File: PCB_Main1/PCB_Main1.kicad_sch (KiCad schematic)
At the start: 32 parts, among them M78AR05-? M78AR05

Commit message: Do annotation
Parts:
- XH3: renamed from J?; value Conn_01x04_Female -> SD-UART
- gave numbers to parts that had none: 24
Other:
- moved on the sheet: XH5, XH6

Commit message: update PCB_Main1 & PCB_Main2
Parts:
- removed M78AR05-3: M78AR05, Converter_DCDC:Converter_DCDC_RECOM_R-78E-0.5_THT, symbol Regulator_Switching:R-78E5.0-0.5
- added UM78AR033-1: R-78E3.3-0.5, Converter_DCDC:Converter_DCDC_RECOM_R-78E-0.5_THT, symbol Regulator_Switching:R-78E3.3-0.5
- XH6: value ICS-UART -> TWELITE_GPS_UART
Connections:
- net GND: now also UM78AR033-1.2 (GND)
- net at D9.2 (A): now also UM78AR033-1.1 (IN)
- net at D13.1 (K): now also UM78AR033-1.3 (OUT)
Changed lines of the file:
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@@
+    )
+  )
+  (symbol (lib_id "Regulator_Switching:R-78E3.3-0.5") (at 68.58 131.445 0) (unit 1)
+    (in_bom yes) (on_board yes) (dnp no) (fields_autoplaced)
+    (property "Reference" "UM78AR033-1" (at 68.58 124.46 0)
+      (effects (font (size 1.27 1.27)))
+    )
+    (property "Value" "R-78E3.3-0.5" (at 68.58 127 0)
+      (effects (font (size 1.27 1.27)))
+    )
+    (property "Footprint" "Converter_DCDC:Converter_DCDC_RECOM_R-78E-0.5_THT" (at 69.85 137.795 0)
+      (effects (font (size 1.27 1.27) italic) (justify left) hide)
+    )
+    (property "Datasheet" "https://www.recom-power.com/pdf/Innoline/R-78Exx-0.5.pdf" (at 68.58 131.445 0)
+      (effects (font (size 1.27 1.27)) hide)
+    )
+    (pin "1")
+    (pin "2")
+    (pin "3")
+    (instances
+      (project "PCB_Main1"
+        (path "/19e4d529-dbb3-4f23-85c8-a29dd0c78a6a"
+          (reference "UM78AR033-1") (unit 1)
+        )
+      )
     )
   )
@@
     )
   )
-  (symbol (lib_id "Regulator_Switching:R-78E5.0-0.5") (at 68.58 131.445 0) (mirror y) (unit 1)
-    (in_bom yes) (on_board yes) (dnp no) (fields_autoplaced)
-    (property "Reference" "M78AR05-3" (at 68.58 125.095 0)
-      (effects (font (size 1.27 1.27)))
-    )
-    (property "Value" "M78AR05" (at 68.58 127.635 0)
-      (effects (font (size 1.27 1.27)))
-    )
-    (property "Footprint" "Converter_DCDC:Converter_DCDC_RECOM_R-78E-0.5_THT" (at 67.31 137.795 0)
-      (effects (font (size 1.27 1.27) italic) (justify left) hide)
-    )
-    (property "Datasheet" "https://www.recom-power.com/pdf/Innoline/R-78Exx-0.5.pdf" (at 68.58 131.445 0)
-      (effects (font (size 1.27 1.27)) hide)
-    )
-    (pin "1")
-    (pin "2")
-    (pin "3")
-    (instances
-      (project "PCB_Main1"
-        (path "/19e4d529-dbb3-4f23-85c8-a29dd0c78a6a"
-          (reference "M78AR05-3") (unit 1)
-        )
-      )
-    )
-  )
   (symbol (lib_id "Regulator_Switching:R-78E5.0-0.5") (at 69.215 36.83 0) (mirror y) (unit 1)
     (in_bom yes) (on_board yes) (dnp no) (fields_autoplaced)
@@
   (symbol (lib_id "Regulator_Switching:R-78E5.0-0.5") (at 68.58 99.695 0) (mirror y) (unit 1)
     (in_bom yes) (on_board yes) (dnp no) (fields_autoplaced)
-    (property "Reference" "M78AR05-2" (at 68.58 93.345 0)
-      (effects (font (size 1.27 1.27)))
-    )
-    (property "Value" "M78AR05" (at 68.58 95.885 0)
+    (property "Reference" "M78AR05-2" (at 68.58 92.71 0)
+      (effects (font (size 1.27 1.27)))
+    )
+    (property "Value" "M78AR05" (at 68.58 95.25 0)
       (effects (font (size 1.27 1.27)))
     )
@@
   )
   (symbol (lib_id "Connector:Conn_01x05_Female") (at 80.01 167.005 0) (mirror y) (unit 1)
-    (in_bom yes) (on_board yes) (dnp no) (fields_autoplaced)
-    (property "Reference" "XH6" (at 78.105 165.735 0)
-      (effects (font (size 1.27 1.27)) (justify left))
-    )
-    (property "Value" "ICS-UART" (at 78.105 168.275 0)
-      (effects (font (size 1.27 1.27)) (justify left))
+    (in_bom yes) (on_board yes) (dnp no)
+    (property "Reference" "XH6" (at 69.215 165.1 0)
+      (effects (font (size 1.27 1.27)))
+    )
+    (property "Value" "TWELITE_GPS_UART" (at 69.215 167.64 0)
+      (effects (font (size 1.27 1.27)))
     )
     (property "Footprint" "" (at 80.01 167.005 0)

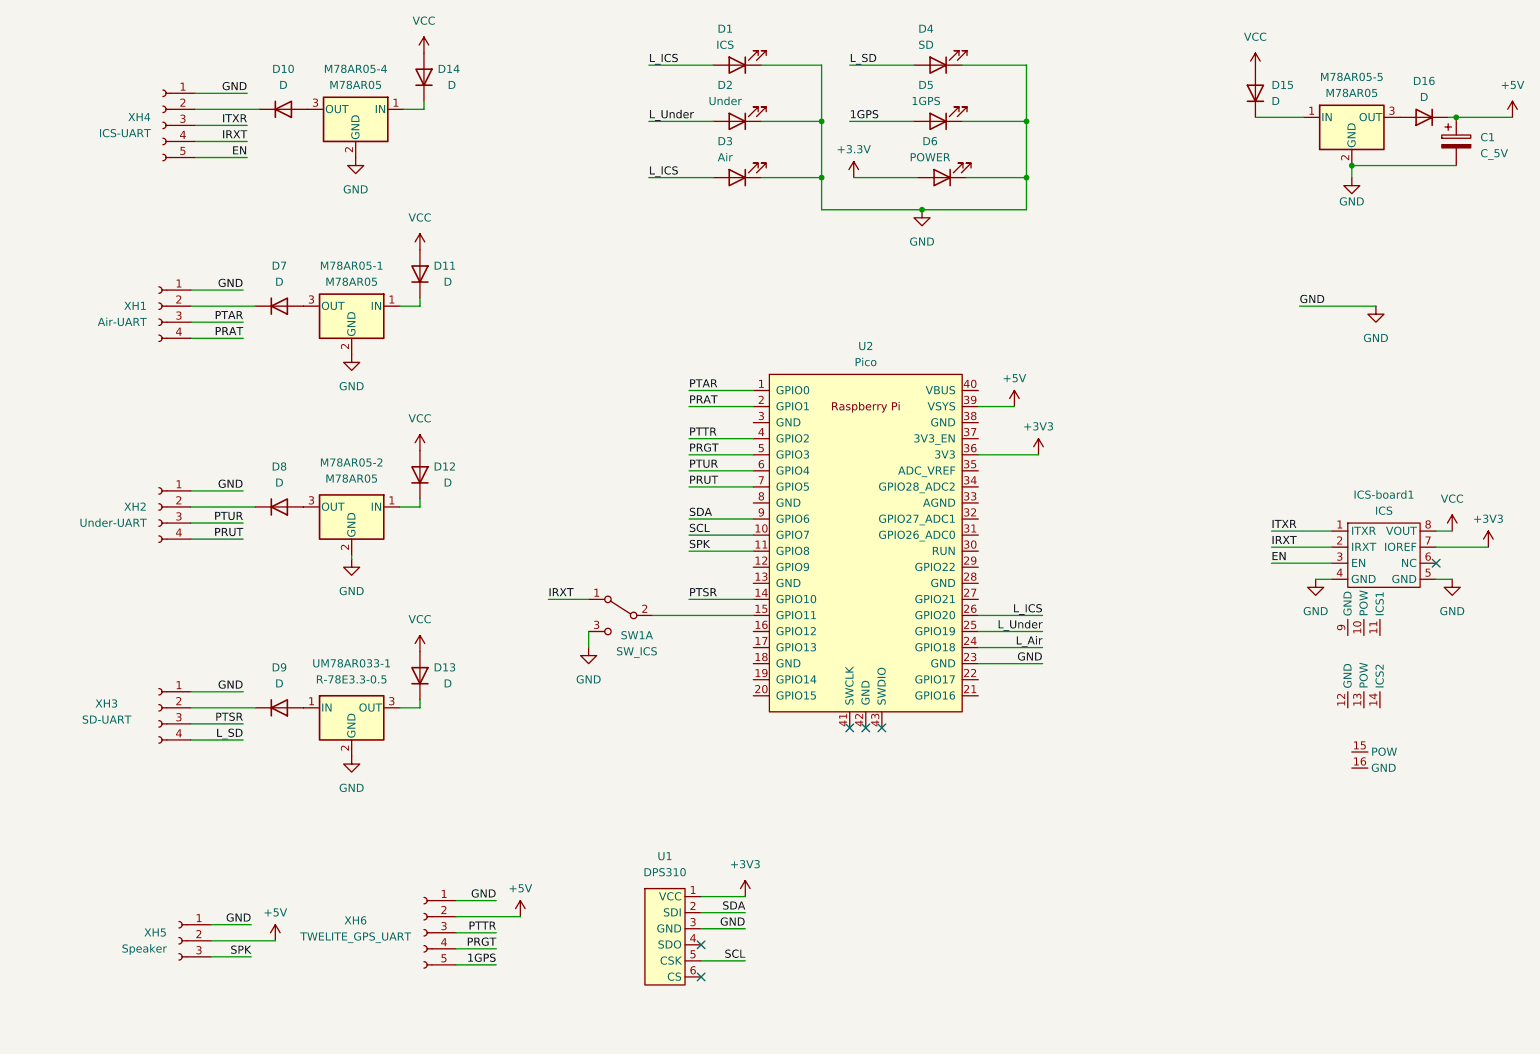
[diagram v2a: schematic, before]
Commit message: add gyro sensor
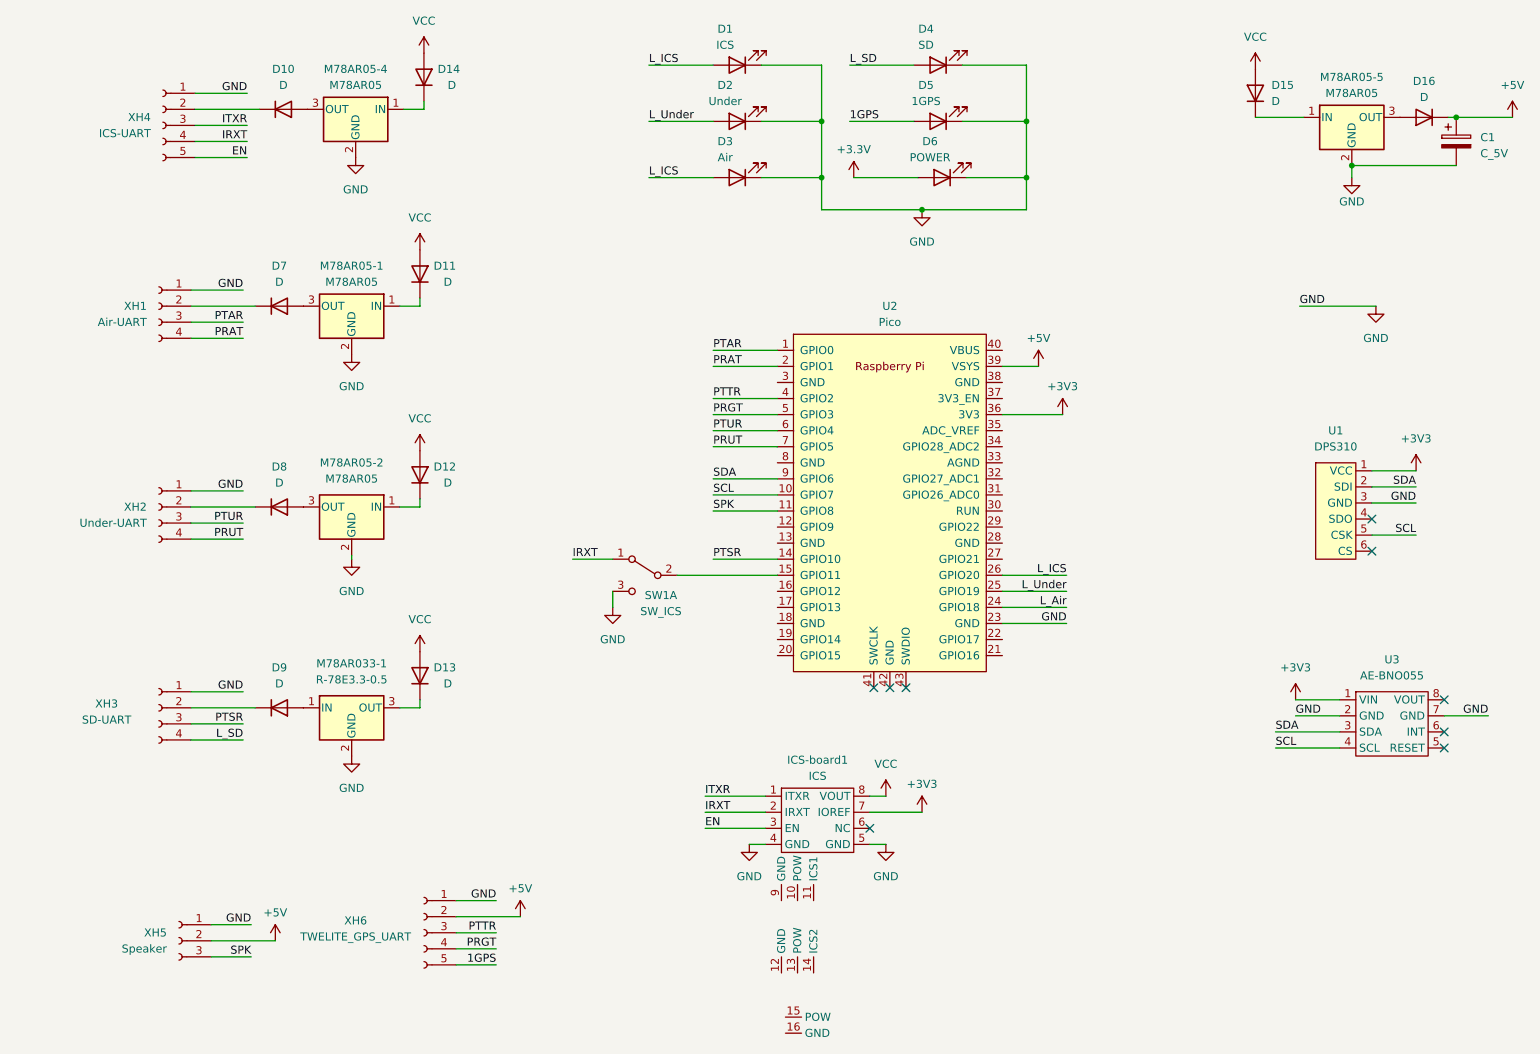
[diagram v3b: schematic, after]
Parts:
- added U3: AE-BNO055, symbol AE-BNO055:AE-BNO055
- renumbered UM78AR033-1 to M78AR033-1
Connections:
- net +3V3: now also U3.1 (VIN)
- net GND: now also U3.2 (GND), U3.7 (GND)
- net SCL: now also U3.4 (SCL)
- net SDA: now also U3.3 (SDA)
- no-connect marks 6 -> 9
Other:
- moved on the sheet: ICS-board1, SW1A, U1, U2

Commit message: update README.md
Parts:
- renumbered D7 to D1, D2 to D10, D3 to D11, D4 to D12, D5 to D13, D6 to D14, D8 to D2, D9 to D3, D10 to D4, D11 to D5, D12 to D6, D13 to D7, D14 to D8, D1 to D9, M78AR05-4 to M78AR05-3, M78AR05-5 to M78AR05-4, U2 to U1, U3 to U2, U1 to U3

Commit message: Update PCB_Main
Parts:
- C1: footprint (none) -> Capacitor_THT:CP_Radial_D5.0mm_P2.50mm
- D1, D15, D16, D2, D3, D4, D5, D6, D7, D8: footprint (none) -> Diode_THT:D_A-405_P10.16mm_Horizontal
- D10, D11, D12, D13, D14, D9: footprint (none) -> LED_THT:LED_D5.0mm
- ICS-board1: footprint (none) -> ICS:ICS
- SW1: footprint (none) -> Connector_PinHeader_2.54mm:PinHeader_1x03_P2.54mm_Vertical
- U1: footprint RPi_Pico:RPi_Pico_SMD_TH -> SamacSys_Parts:RPi_Pico_SMD_TH
- U2: footprint (none) -> AE-BNO055:AE-BNO055
- U3: footprint (none) -> DPS310:DPS310
- XH1, XH2, XH3: footprint (none) -> Connector_JST:JST_XH_S4B-XH-A_1x04_P2.50mm_Horizontal
- XH4, XH6: footprint (none) -> Connector_JST:JST_XH_S5B-XH-A_1x05_P2.50mm_Horizontal
- XH5: footprint (none) -> Connector_JST:JST_XH_S3B-XH-A_1x03_P2.50mm_Horizontal
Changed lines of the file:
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@@
       (effects (font (size 1.27 1.27)))
     )
-    (property "Footprint" "" (at 129.54 29.845 0)
+    (property "Footprint" "LED_THT:LED_D5.0mm" (at 129.54 29.845 0)
       (effects (font (size 1.27 1.27)) hide)
     )
@@
       (effects (font (size 1.27 1.27)))
     )
-    (property "Footprint" "" (at 57.15 131.445 0)
+    (property "Footprint" "Diode_THT:D_A-405_P10.16mm_Horizontal" (at 57.15 131.445 0)
       (effects (font (size 1.27 1.27)) hide)
     )
@@
       (effects (font (size 1.27 1.27)))
     )
-    (property "Footprint" "" (at 133.985 141.605 0)
+    (property "Footprint" "ICS:ICS" (at 133.985 141.605 0)
       (effects (font (size 1.27 1.27)) hide)
     )
@@
       (effects (font (size 1.27 1.27)) (justify right))
     )
-    (property "Footprint" "" (at 79.375 126.365 0)
+    (property "Footprint" "Diode_THT:D_A-405_P10.16mm_Horizontal" (at 79.375 126.365 0)
       (effects (font (size 1.27 1.27)) hide)
     )
@@
       (effects (font (size 1.27 1.27)))
     )
-    (property "Footprint" "" (at 38.1 131.445 0)
+    (property "Footprint" "Connector_JST:JST_XH_S4B-XH-A_1x04_P2.50mm_Horizontal" (at 38.1 131.445 0)
       (effects (font (size 1.27 1.27)) hide)
     )
@@
       (effects (font (size 1.27 1.27)) (justify left))
     )
-    (property "Footprint" "" (at 41.275 168.275 0)
+    (property "Footprint" "Connector_JST:JST_XH_S3B-XH-A_1x03_P2.50mm_Horizontal" (at 41.275 168.275 0)
       (effects (font (size 1.27 1.27)) hide)
     )
@@
       (effects (font (size 1.27 1.27)))
     )
-    (property "Footprint" "" (at 57.15 67.945 0)
+    (property "Footprint" "Diode_THT:D_A-405_P10.16mm_Horizontal" (at 57.15 67.945 0)
       (effects (font (size 1.27 1.27)) hide)
     )
@@
       (effects (font (size 1.27 1.27)))
     )
-    (property "Footprint" "" (at 236.22 99.06 0)
+    (property "Footprint" "DPS310:DPS310" (at 236.22 99.06 0)
       (effects (font (size 1.27 1.27)) hide)
     )
@@
       (effects (font (size 1.27 1.27)) (justify left))
     )
-    (property "Footprint" "" (at 38.1 67.945 0)
+    (property "Footprint" "Connector_JST:JST_XH_S4B-XH-A_1x04_P2.50mm_Horizontal" (at 38.1 67.945 0)
       (effects (font (size 1.27 1.27)) hide)
     )
@@
       (effects (font (size 1.27 1.27)) (justify right))
     )
-    (property "Footprint" "" (at 79.375 94.615 0)
+    (property "Footprint" "Diode_THT:D_A-405_P10.16mm_Horizontal" (at 79.375 94.615 0)
       (effects (font (size 1.27 1.27)) hide)
     )
@@
       (effects (font (size 1.27 1.27)) (justify right))
     )
-    (property "Footprint" "" (at 211.455 34.29 0)
+    (property "Footprint" "Diode_THT:D_A-405_P10.16mm_Horizontal" (at 211.455 34.29 0)
       (effects (font (size 1.27 1.27)) hide)
     )
@@
       (effects (font (size 1.27 1.27)))
     )
-    (property "Footprint" "" (at 114.935 110.49 0)
+    (property "Footprint" "Connector_PinHeader_2.54mm:PinHeader_1x03_P2.54mm_Vertical" (at 114.935 110.49 0)
       (effects (font (size 1.27 1.27)) hide)
     )
@@
       (effects (font (size 1.27 1.27)) (justify left))
     )
-    (property "Footprint" "" (at 38.735 39.37 0)
+    (property "Footprint" "Connector_JST:JST_XH_S5B-XH-A_1x05_P2.50mm_Horizontal" (at 38.735 39.37 0)
       (effects (font (size 1.27 1.27)) hide)
     )
@@
       (effects (font (size 1.27 1.27)))
     )
-    (property "Footprint" "" (at 80.01 167.005 0)
+    (property "Footprint" "Connector_JST:JST_XH_S5B-XH-A_1x05_P2.50mm_Horizontal" (at 80.01 167.005 0)
       (effects (font (size 1.27 1.27)) hide)
     )
@@
       (effects (font (size 1.27 1.27)) (justify left))
     )
-    (property "Footprint" "" (at 244.1702 45.72 0)
+    (property "Footprint" "Capacitor_THT:CP_Radial_D5.0mm_P2.50mm" (at 244.1702 45.72 0)
       (effects (font (size 1.27 1.27)) hide)
     )
@@
       (effects (font (size 1.27 1.27)))
     )
-    (property "Footprint" "" (at 129.54 47.625 0)
+    (property "Footprint" "LED_THT:LED_D5.0mm" (at 129.54 47.625 0)
       (effects (font (size 1.27 1.27)) hide)
     )
@@
       (effects (font (size 1.27 1.27)))
     )
-    (property "Footprint" "" (at 161.29 29.845 0)
+    (property "Footprint" "LED_THT:LED_D5.0mm" (at 161.29 29.845 0)
       (effects (font (size 1.27 1.27)) hide)
     )
@@
       (effects (font (size 1.27 1.27)) (justify right))
     )
-    (property "Footprint" "" (at 79.375 62.865 0)
+    (property "Footprint" "Diode_THT:D_A-405_P10.16mm_Horizontal" (at 79.375 62.865 0)
       (effects (font (size 1.27 1.27)) hide)
     )
@@
       (effects (font (size 1.27 1.27)))
     )
-    (property "Footprint" "" (at 161.925 47.625 0)
+    (property "Footprint" "LED_THT:LED_D5.0mm" (at 161.925 47.625 0)
       (effects (font (size 1.27 1.27)) hide)
     )
@@
       (effects (font (size 1.27 1.27)))
     )
-    (property "Footprint" "" (at 129.54 38.735 0)
+    (property "Footprint" "LED_THT:LED_D5.0mm" (at 129.54 38.735 0)
       (effects (font (size 1.27 1.27)) hide)
     )
@@
       (effects (font (size 1.27 1.27)))
     )
-    (property "Footprint" "" (at 57.15 99.695 0)
+    (property "Footprint" "Diode_THT:D_A-405_P10.16mm_Horizontal" (at 57.15 99.695 0)
       (effects (font (size 1.27 1.27)) hide)
     )
@@
       (effects (font (size 1.27 1.27)))
     )
-    (property "Footprint" "" (at 161.29 38.735 0)
+    (property "Footprint" "LED_THT:LED_D5.0mm" (at 161.29 38.735 0)
       (effects (font (size 1.27 1.27)) hide)
     )
@@
       (effects (font (size 1.27 1.27)))
     )
-    (property "Footprint" "" (at 57.785 36.83 0)
+    (property "Footprint" "Diode_THT:D_A-405_P10.16mm_Horizontal" (at 57.785 36.83 0)
       (effects (font (size 1.27 1.27)) hide)
     )
@@
       (effects (font (size 1.27 1.27)))
     )
-    (property "Footprint" "" (at 224.79 127.635 0)
+    (property "Footprint" "AE-BNO055:AE-BNO055" (at 224.79 127.635 0)
       (effects (font (size 1.27 1.27)) hide)
     )
@@
       (effects (font (size 1.27 1.27)) (justify right))
     )
-    (property "Footprint" "" (at 80.01 31.75 0)
+    (property "Footprint" "Diode_THT:D_A-405_P10.16mm_Horizontal" (at 80.01 31.75 0)
       (effects (font (size 1.27 1.27)) hide)
     )
@@
       (effects (font (size 1.27 1.27)) (justify left))
     )
-    (property "Footprint" "" (at 38.1 99.695 0)
+    (property "Footprint" "Connector_JST:JST_XH_S4B-XH-A_1x04_P2.50mm_Horizontal" (at 38.1 99.695 0)
       (effects (font (size 1.27 1.27)) hide)
     )
@@
       (effects (font (size 1.27 1.27)))
     )
-    (property "Footprint" "" (at 238.125 38.1 0)
+    (property "Footprint" "Diode_THT:D_A-405_P10.16mm_Horizontal" (at 238.125 38.1 0)
       (effects (font (size 1.27 1.27)) hide)
     )
@@
       (effects (font (size 1.27 1.27)))
     )
-    (property "Footprint" "RPi_Pico:RPi_Pico_SMD_TH" (at 153.67 99.06 90)
-      (effects (font (size 1.27 1.27)) hide)
-    )
+    (property "Footprint" "SamacSys_Parts:RPi_Pico_SMD_TH" (at 153.67 99.06 90)
+      (effects (font (size 1.27 1.27)) hide)
+    )
